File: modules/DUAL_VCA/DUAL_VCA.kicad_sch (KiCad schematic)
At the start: 58 parts, among them IC1 CA3084, IC2 µA741C, IC3 µA741C, IC4 µA741C, IC5 µA741C, IC6 CA3080, IC7 CA3080, IC8 µA741C, P1 100k, P2 100k, P3 1k, P4 10k, P5 100k, P6 4k7, P7 100k, P8 100k, T1 BC177C

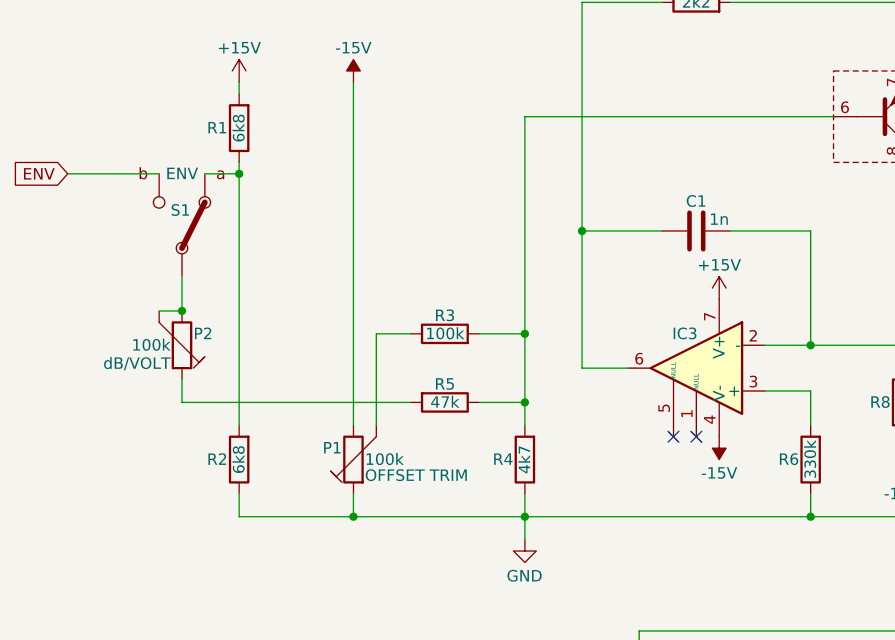
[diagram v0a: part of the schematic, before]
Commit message: dual vca pcb traces
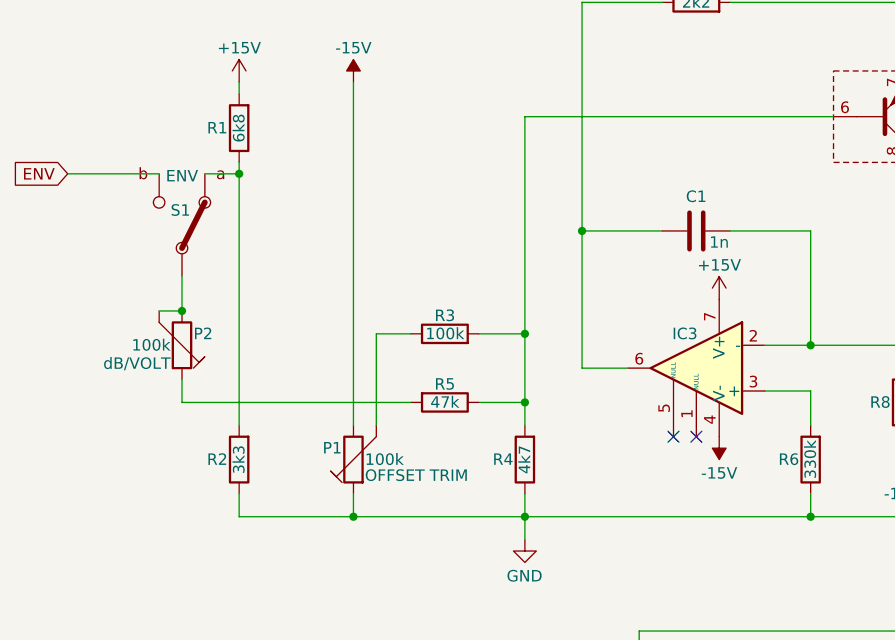
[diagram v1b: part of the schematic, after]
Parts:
- C1, C6: footprint FormantKO:C_Rect -> FormantKO:C_Rect_300_400
- C2, C3: footprint FormantKO:C_Rect -> FormantKO:C_Rect_400_500
- R2: value 6k8 -> 3k3
- S1: Legend (none) -> ENV
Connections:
- net at IC3.6, R7.1: now also C1.2; no longer C1.1
- net at IC1.8, IC3.2 (-), R8.2: now also C1.1; no longer C1.2
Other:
- moved on the sheet: C1
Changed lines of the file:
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@@
 			)
 		)
-		(property "Footprint" "FormantKO:C_Rect"
+		(property "Footprint" "FormantKO:C_Rect_400_500"
 			(at 31.75 127 0)
 			(hide yes)
@@
 	(symbol
 		(lib_id "FormantKO:C")
-		(at 95.25 57.15 90)
+		(at 95.25 57.15 270)
 		(unit 1)
 		(body_style 1)
@@
 		(dnp no)
 		(property "Reference" "C1"
-			(at 95.25 54.61 90)
+			(at 95.25 53.34 90)
 			(show_name no)
 			(do_not_autoplace no)
@@
 					(size 1.27 1.27)
 				)
-				(justify top)
 			)
 		)
 		(property "Value" "1n"
-			(at 97.79 55.88 90)
+			(at 97.79 58.42 90)
 			(show_name no)
 			(do_not_autoplace no)
@@
 			)
 		)
-		(property "Footprint" "FormantKO:C_Rect"
+		(property "Footprint" "FormantKO:C_Rect_300_400"
 			(at 95.25 57.15 0)
 			(hide yes)
@@
 			)
 		)
-		(property "Value" "6k8"
+		(property "Value" "3k3"
 			(at 44.45 82.55 0)
 			(show_name no)
@@
 			)
 		)
-		(property "Footprint" "FormantKO:C_Rect"
+		(property "Footprint" "FormantKO:C_Rect_300_400"
 			(at 190.5 57.15 0)
 			(hide yes)
@@
 		(property "Value" "ENV"
 			(at 38.1 50.8 0)
+			(hide yes)
 			(show_name no)
 			(do_not_autoplace no)
@@
 			)
 		)
+		(property "Legend" "ENV"
+			(at 38.1 51.054 0)
+			(show_name no)
+			(do_not_autoplace no)
+			(effects
+				(font
+					(size 1.27 1.27)
+				)
+			)
+		)
 		(pin "2"
 		)
@@
 			)
 		)
-		(property "Footprint" "FormantKO:C_Rect"
+		(property "Footprint" "FormantKO:C_Rect_400_500"
 			(at 31.75 114.3 0)
 			(hide yes)
